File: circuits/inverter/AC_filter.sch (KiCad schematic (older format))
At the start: 0 parts

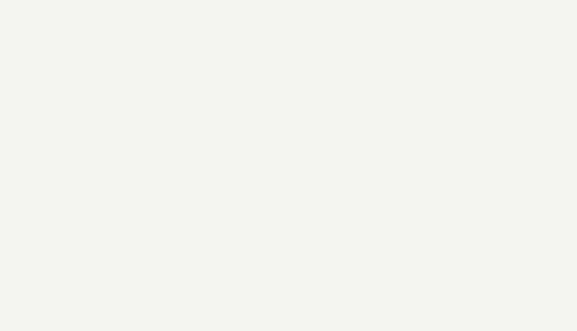
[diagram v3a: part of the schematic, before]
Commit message: bulk-updates libraries and schematics
schematic is updated to Kicad 5.1.14
updates various sheets with new circuits
adds various component libraries
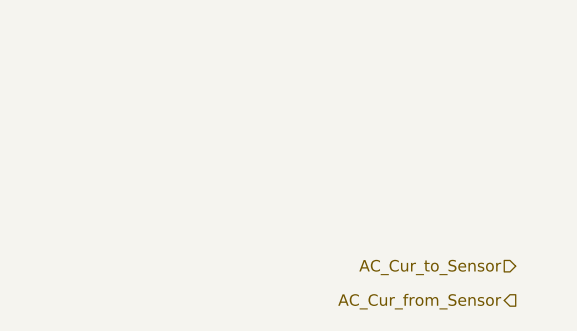
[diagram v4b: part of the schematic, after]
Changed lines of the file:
@@
-EESchema Schematic File Version 2
-LIBS:lm317
-LIBS:kv30f
-LIBS:OSSI_standard_components
-LIBS:connectors
-LIBS:lm4030
-LIBS:acs722
+EESchema Schematic File Version 4
 LIBS:OSSI_MK_I-cache
-EELAYER 25 0
+EELAYER 30 0
 EELAYER END
 $Descr A4 11693 8268
@@
 Text HLabel 1150 950  0    60   Input ~ 0
 AC_Vtg_L
+Text HLabel 10975 5275 0    50   Output ~ 0
+AC_Cur_from_Sensor
+Text HLabel 10975 5125 0    50   Input ~ 0
+AC_Cur_to_Sensor
 $EndSCHEMATC
